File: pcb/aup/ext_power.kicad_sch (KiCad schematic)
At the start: 27 parts, among them J201 Barral_Jack_12V, J202 USB_C_Receptacle_USB2.0_16P, Q201 AO3401A, Q202 AO3401A, U201 USBLC6-2SC6, U202 TPS563257DRLR

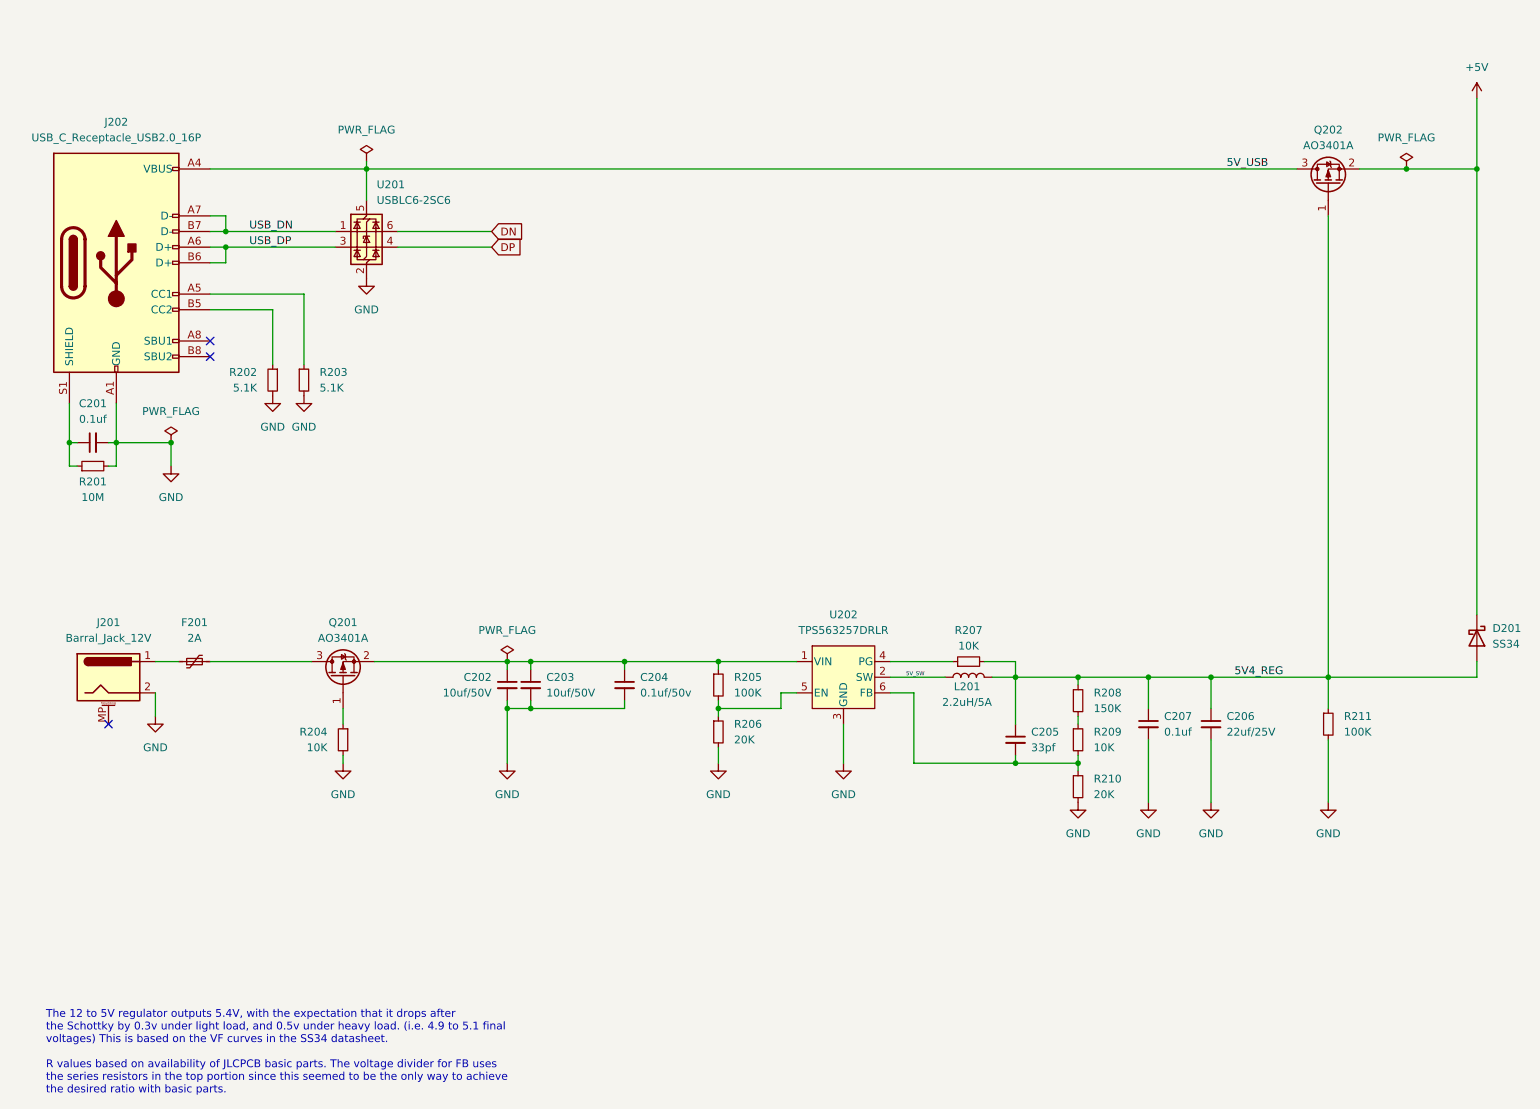
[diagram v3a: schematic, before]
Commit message: Added symbols for the major components
It should be possible to do a first pass placement of ICs on the pcb as
a rough fit check.

Most imported footprints are still missing models.
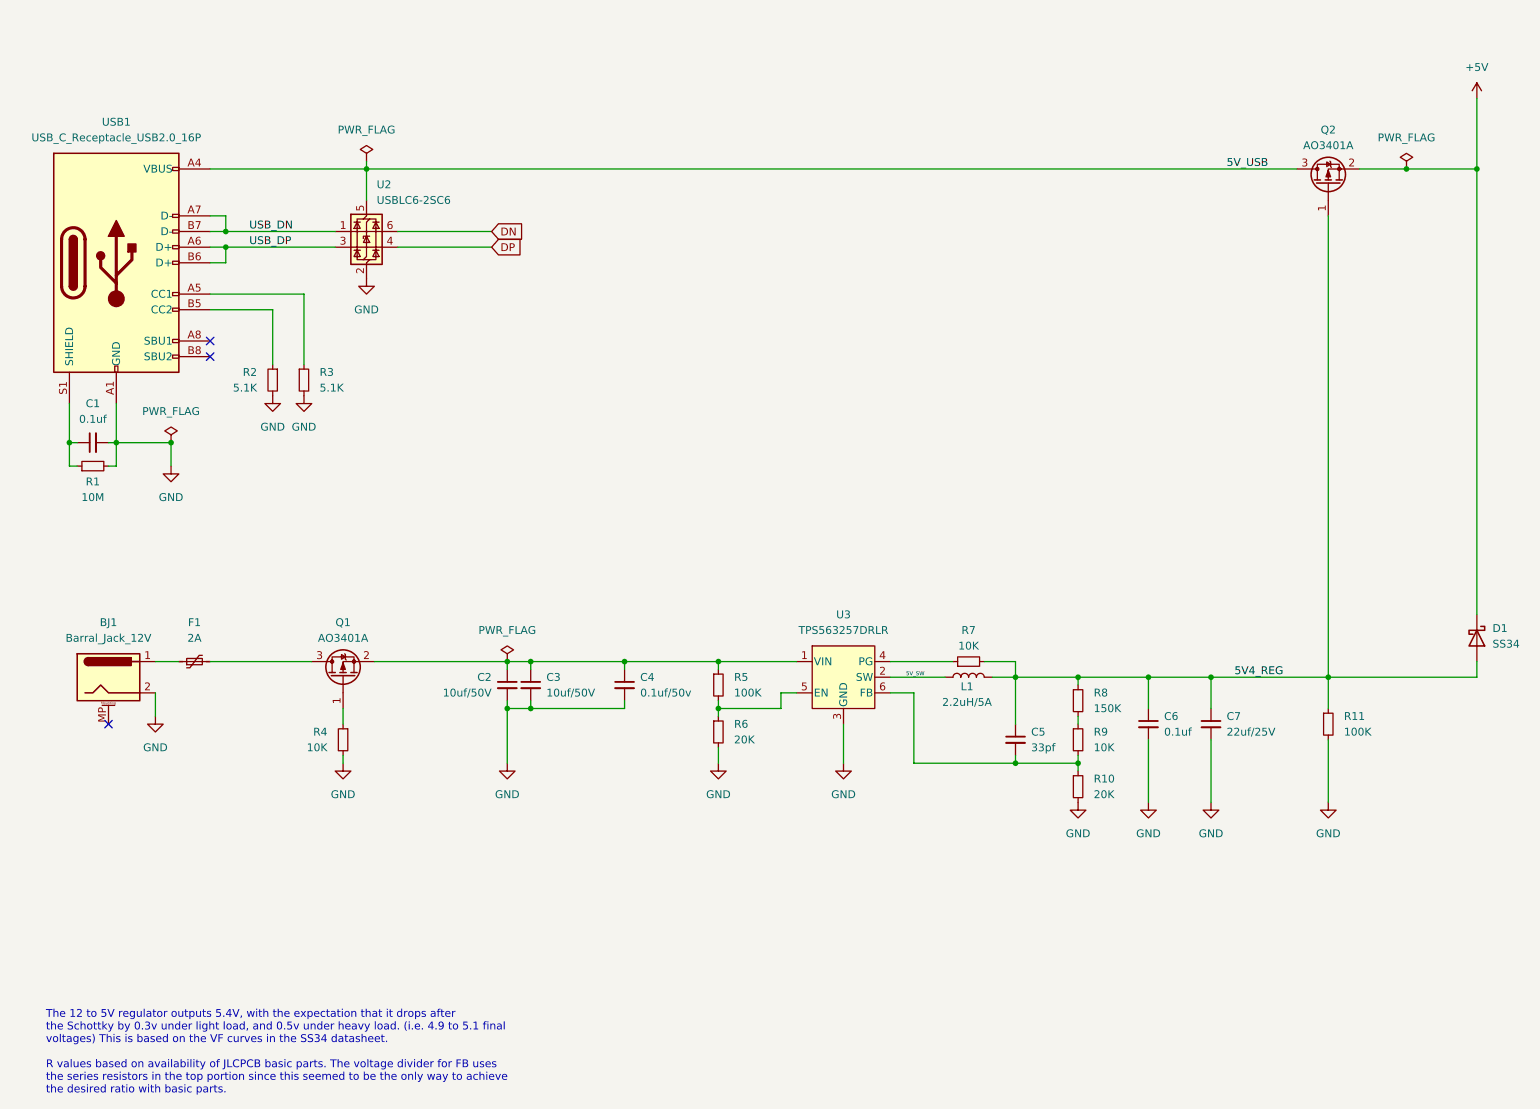
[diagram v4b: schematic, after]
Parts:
- U3: renamed from U202; footprint SOT6_DRL_TEX -> !Misc:SOT6_DRL_TEX
- renumbered J201 to BJ1, C201 to C1, C202 to C2, C203 to C3, C204 to C4, C205 to C5, C207 to C6, C206 to C7, D201 to D1, F201 to F1, L201 to L1, Q201 to Q1, Q202 to Q2, R201 to R1, R210 to R10, R211 to R11, R202 to R2, R203 to R3, R204 to R4, R205 to R5, R206 to R6, R207 to R7, R208 to R8, R209 to R9, U201 to U2, J202 to USB1

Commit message: First pass on upper voltage rails
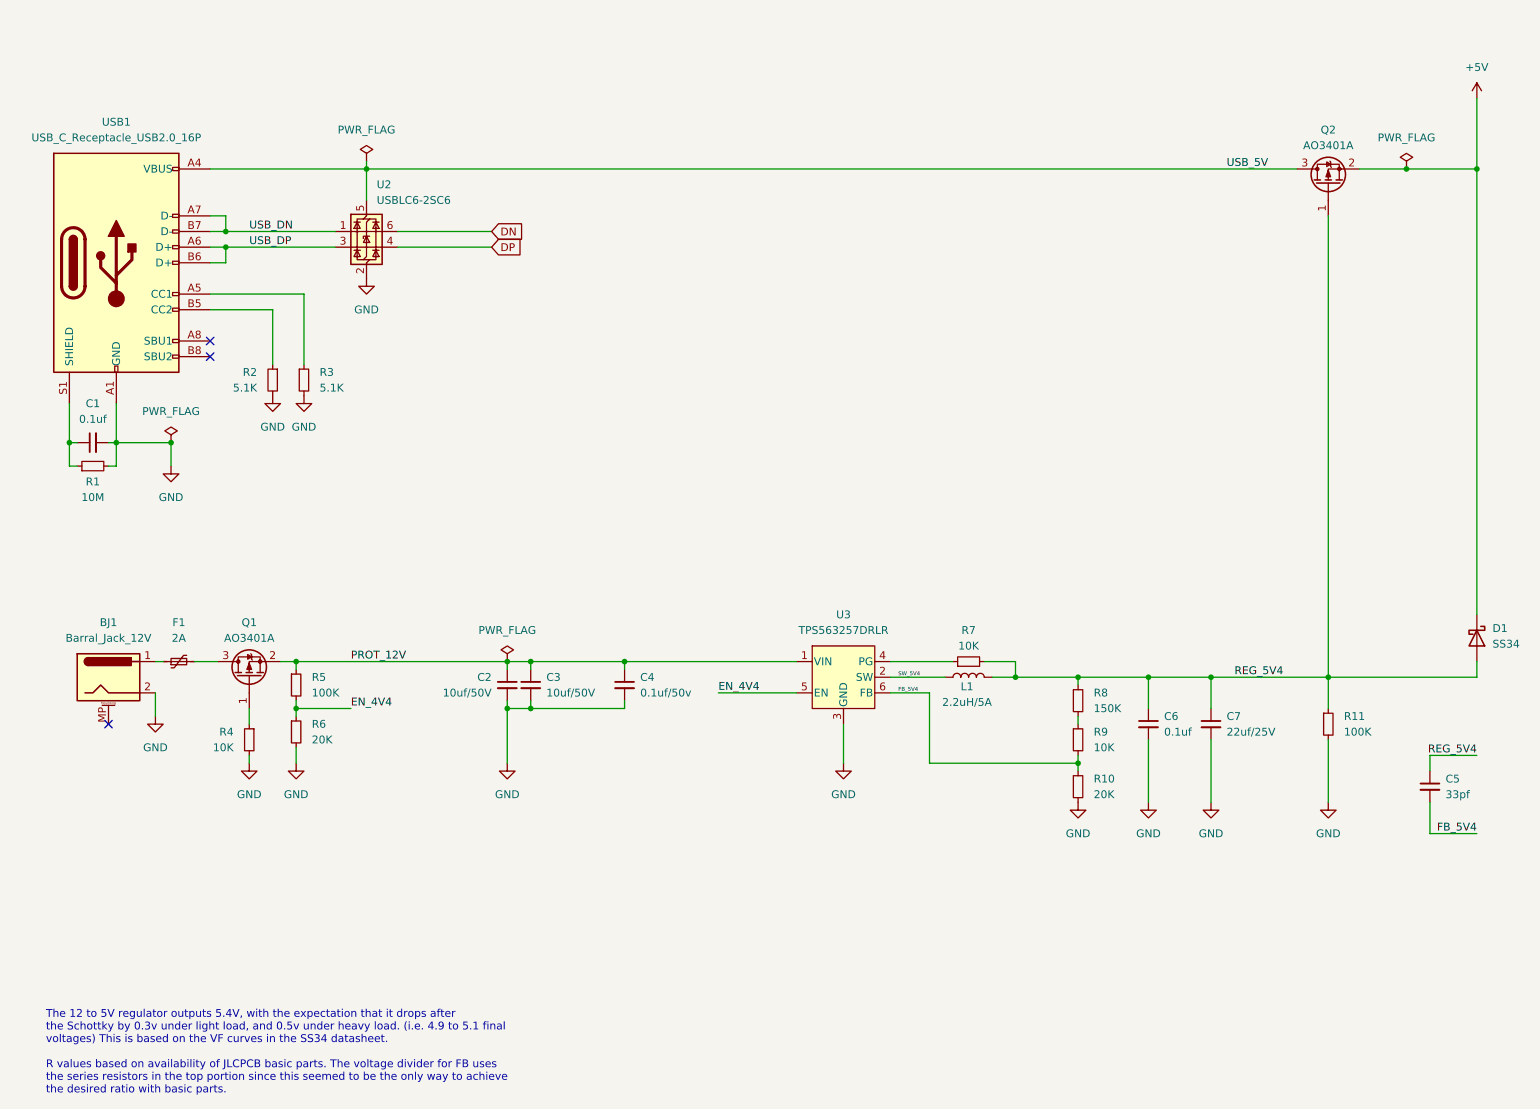
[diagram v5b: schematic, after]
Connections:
- net PROT_12V: now reaches C2.1, C3.1, C4.1, Q1.2 (S), R5.1, U3.1 (VIN)
- net EN_4V4: now reaches R5.2, R6.1, U3.5 (EN)
- net FB_5V4: now reaches C5.2, R10.1, R9.2, U3.6 (FB)
- net 5V4_REG renamed REG_5V4
- net 5V_SW renamed SW_5V4
- net 5V_USB renamed USB_5V
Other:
- moved on the sheet: C5, F1, Q1, R4, R5, R6
